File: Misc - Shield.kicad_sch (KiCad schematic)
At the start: 9 parts

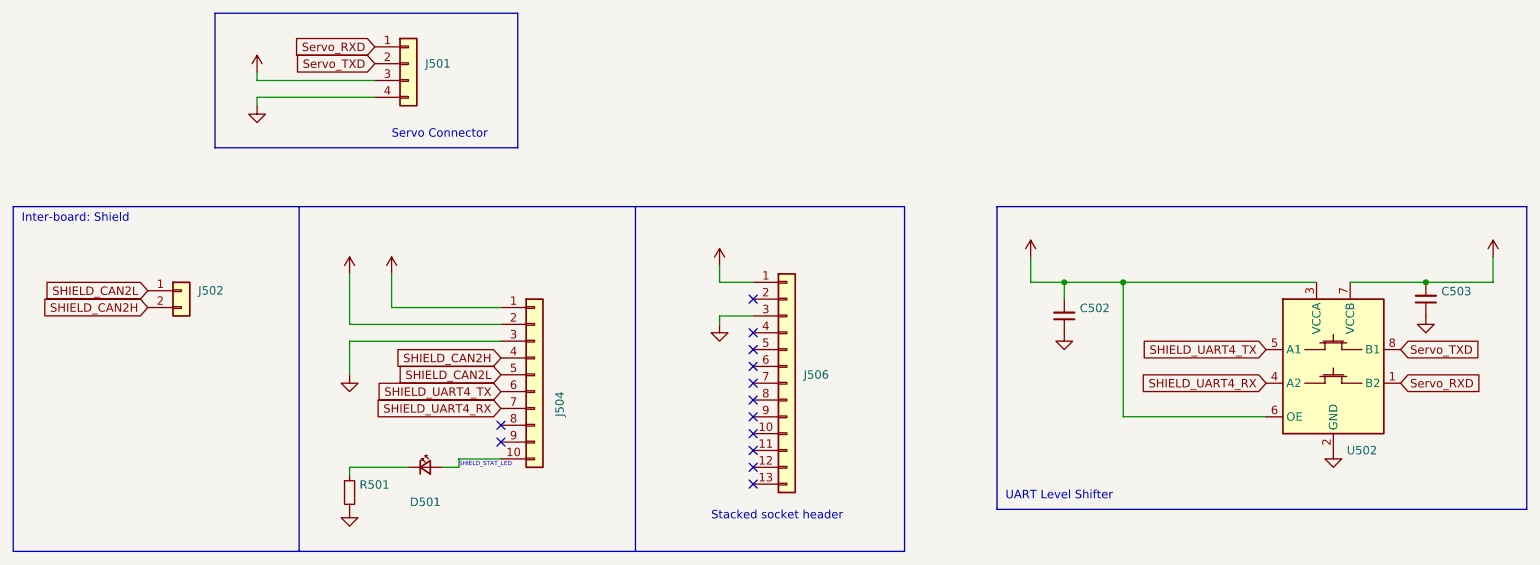
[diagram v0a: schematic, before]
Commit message: incorporated rework into official design
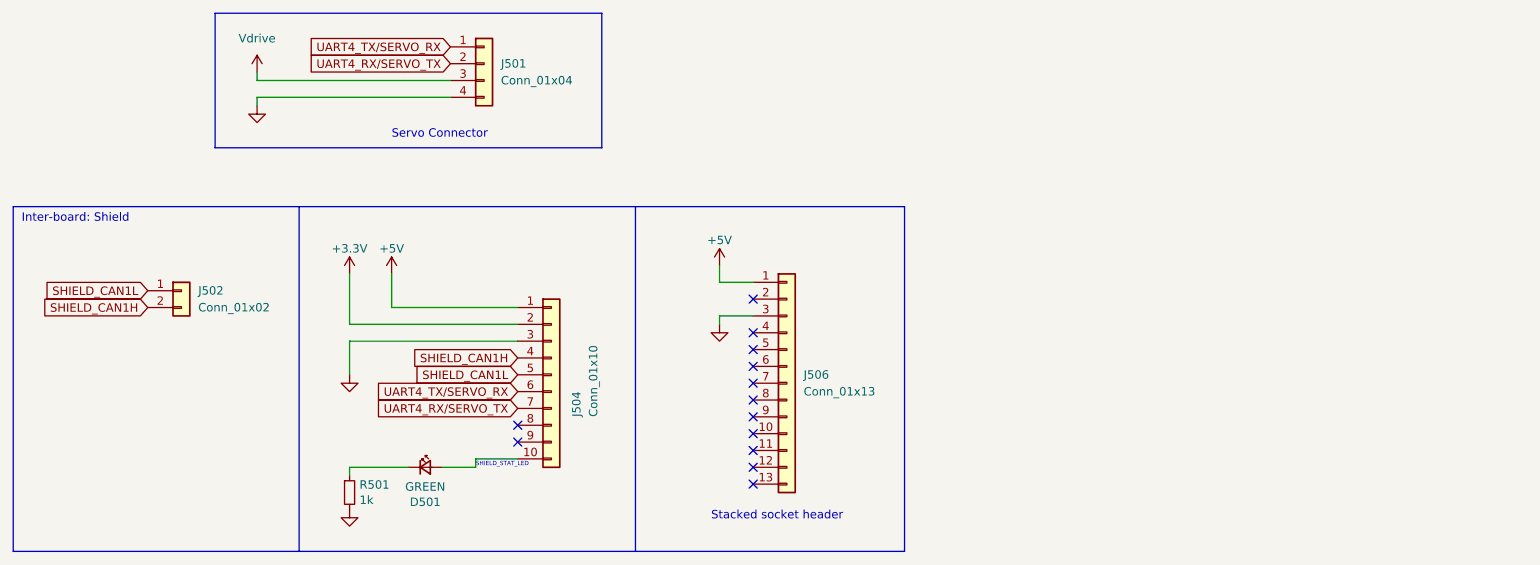
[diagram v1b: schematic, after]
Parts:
- removed C502, C503: (no value), symbol Device:C_Small
- removed U502: (no value), symbol Logic_LevelTranslator:TXS0102DCU
- D501: value (none) -> GREEN; footprint (none) -> LED_SMD:LED_0603_1608Metric
- J501: value (none) -> Conn_01x04; footprint (none) -> SnapEDA Library:JST_B4B-XH-A(LF)(SN)
- J502: value (none) -> Conn_01x02; footprint (none) -> SnapEDA Library:JST_B2B-XH-A(LF)(SN)
- J504: value (none) -> Conn_01x10; footprint (none) -> Connector_PinSocket_2.54mm:PinSocket_1x10_P2.54mm_Vertical
- J506: value (none) -> Conn_01x13; footprint (none) -> Connector_PinSocket_2.54mm:PinSocket_1x13_P2.54mm_Vertical
- R501: value (none) -> 1k; footprint (none) -> Resistor_SMD:R_0402_1005Metric
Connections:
- net Servo_RXD is gone; now on net UART4_TX/SERVO_RX: J501.1 (Pin_1)
- net Servo_TXD is gone; now on net UART4_RX/SERVO_TX: J501.2 (Pin_2)
- net SHIELD_CAN2H renamed SHIELD_CAN1H
- net SHIELD_CAN2L renamed SHIELD_CAN1L
- net SHIELD_UART4_RX renamed UART4_RX/SERVO_TX
- net SHIELD_UART4_TX renamed UART4_TX/SERVO_RX
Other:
- note removed: "UART Level Shifter"
- moved on the sheet: J501, J504
